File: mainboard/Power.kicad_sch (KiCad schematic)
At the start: 34 parts, among them IC801 LP5907MFX-2.8, IC802 LP5907MFX-1.5, IC803 TPS62823DLC, IC804 LP5907MFX-3.0, IC805 LP5907MFX-2.8, IC806 LP5907MFX-1.2, SW801 On / Off

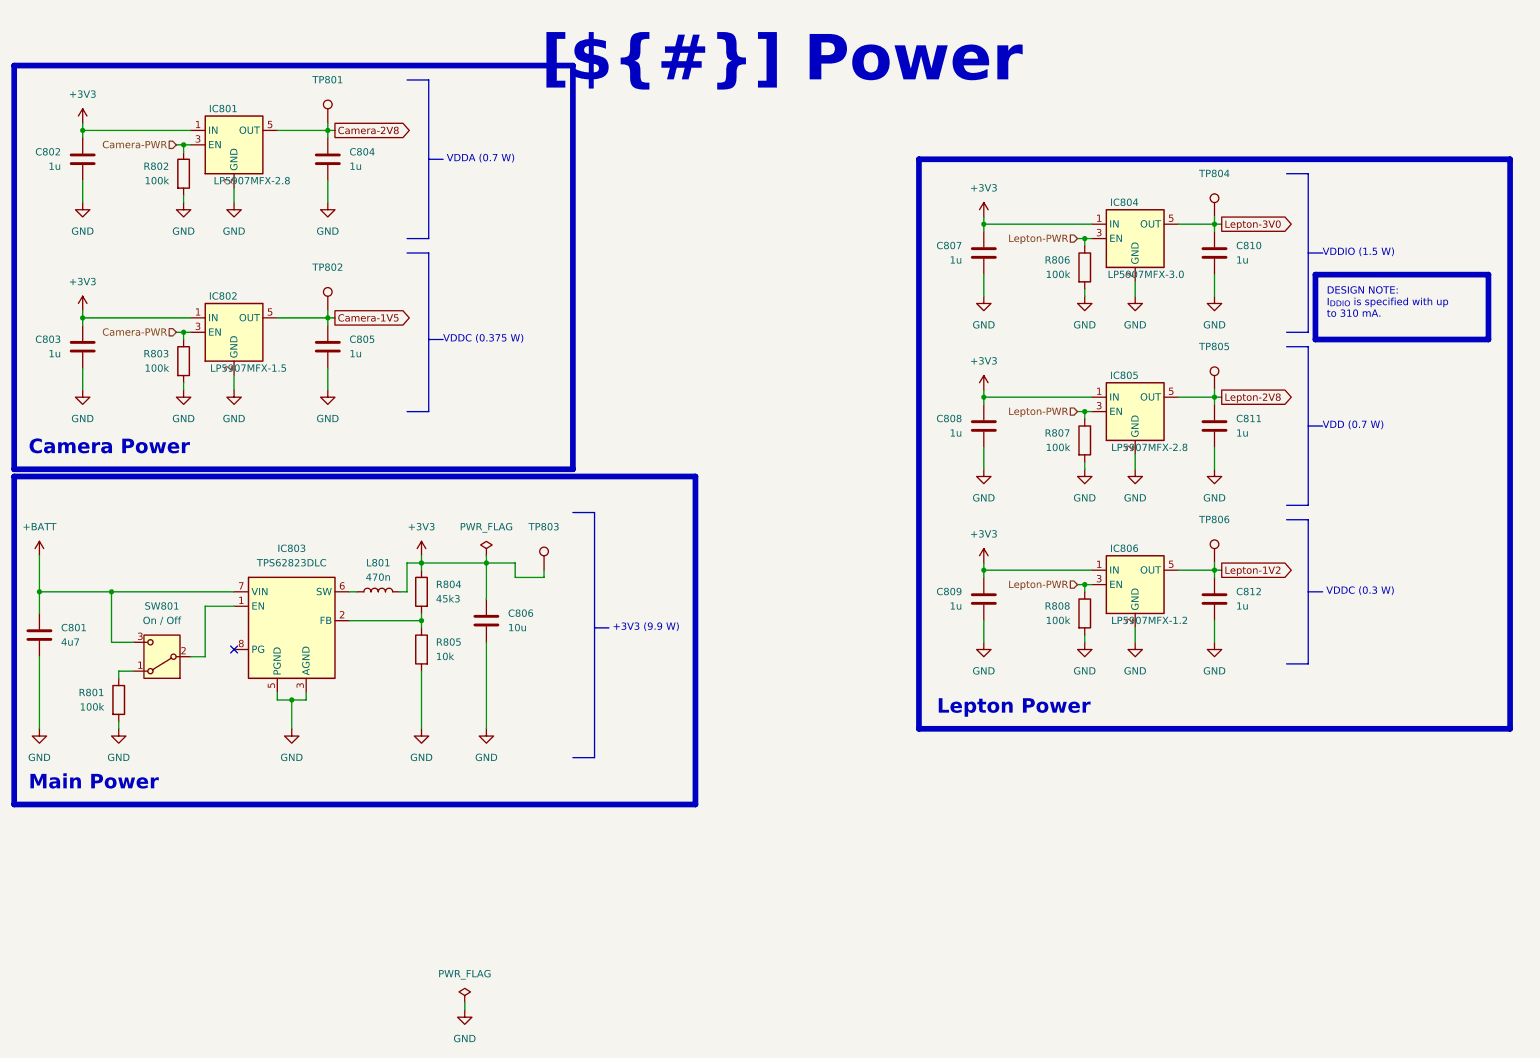
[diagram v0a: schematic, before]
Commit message: Changed: Fix different minor assembly ToDos
Signed-off-by: Daniel Kampert <DanielKampert@kampis-elektroecke.de>
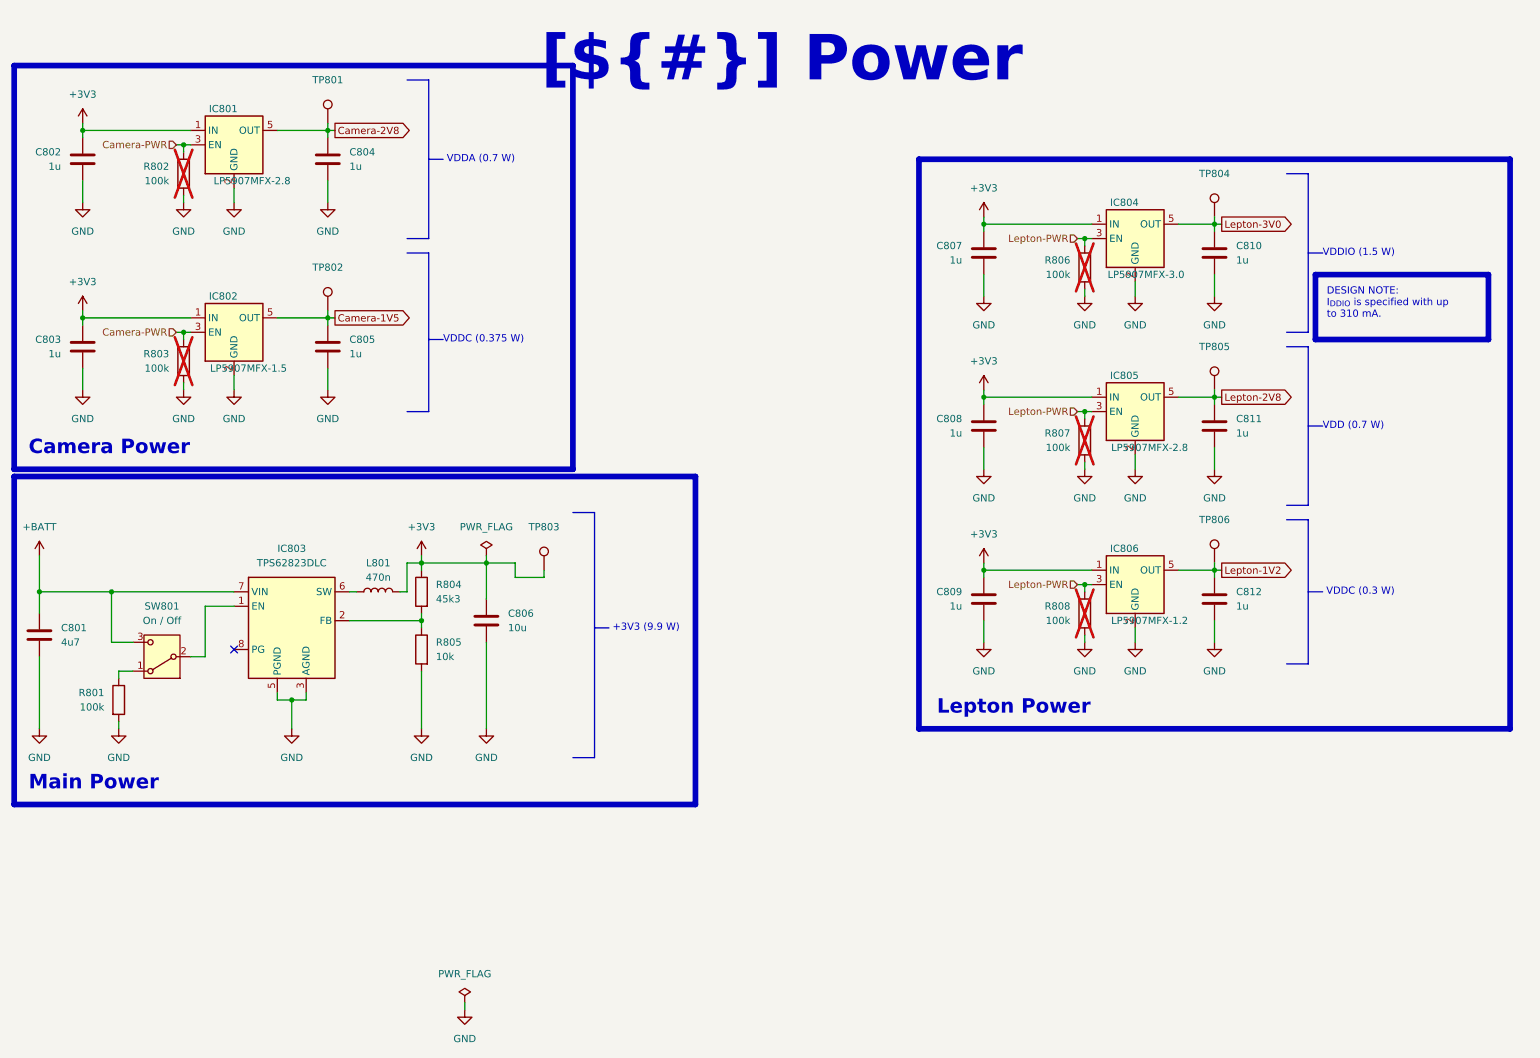
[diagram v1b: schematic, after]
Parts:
- C801: manf# 0603ZG475ZAT2A -> 06036D475MAT4A; mouser# 581-0603ZG475ZAT2A -> 581-06036D475MAT4A
- C806: manf# 0603YD106MAT2A -> 06034D106KAT2A; mouser# 581-0603YD106MAT2A -> 581-06034D106K
- R802, R803, R806, R807, R808: now not fitted; now left out of the parts list
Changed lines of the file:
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@@
 			)
 		)
-		(property "Datasheet" "https://datasheets.kyocera-avx.com/KGM_Y5V.pdf"
+		(property "Datasheet" "https://datasheets.kyocera-avx.com/cx5r.pdf"
 			(at 17.78 124.46 0)
 			(effects
@@
 			)
 		)
-		(property "manf#" "0603ZG475ZAT2A"
+		(property "manf#" "06036D475MAT4A"
 			(at 17.78 124.46 0)
 			(effects
@@
 			)
 		)
-		(property "mouser#" "581-0603ZG475ZAT2A"
+		(property "mouser#" "581-06036D475MAT4A"
 			(at 17.78 124.46 0)
 			(effects
@@
 		(unit 1)
 		(exclude_from_sim no)
-		(in_bom yes)
+		(in_bom no)
 		(on_board yes)
-		(dnp no)
+		(dnp yes)
 		(property "Reference" "R806"
 			(at 199.39 58.42 0)
@@
 		(unit 1)
 		(exclude_from_sim no)
-		(in_bom yes)
+		(in_bom no)
 		(on_board yes)
-		(dnp no)
+		(dnp yes)
 		(property "Reference" "R808"
 			(at 199.39 119.38 0)
@@
 			)
 		)
-		(property "Datasheet" "https://datasheets.kyocera-avx.com/cx5r-KGM.pdf"
+		(property "Datasheet" "https://datasheets.kyocera-avx.com/cx5r.pdf"
 			(at 96.52 121.92 0)
 			(effects
@@
 			)
 		)
-		(property "manf#" "0603YD106MAT2A"
+		(property "manf#" "06034D106KAT2A"
 			(at 96.52 121.92 0)
 			(effects
@@
 			)
 		)
-		(property "mouser#" "581-0603YD106MAT2A"
+		(property "mouser#" "581-06034D106K"
 			(at 96.52 121.92 0)
 			(effects
@@
 		(unit 1)
 		(exclude_from_sim no)
-		(in_bom yes)
+		(in_bom no)
 		(on_board yes)
-		(dnp no)
+		(dnp yes)
 		(property "Reference" "R802"
 			(at 40.64 41.91 0)
@@
 		(unit 1)
 		(exclude_from_sim no)
-		(in_bom yes)
+		(in_bom no)
 		(on_board yes)
-		(dnp no)
+		(dnp yes)
 		(property "Reference" "R803"
 			(at 40.64 74.93 0)
@@
 		(unit 1)
 		(exclude_from_sim no)
-		(in_bom yes)
+		(in_bom no)
 		(on_board yes)
-		(dnp no)
+		(dnp yes)
 		(property "Reference" "R807"
 			(at 199.39 88.9 0)

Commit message: Update to KiCad 10
Closes: #31, #29, #27

Signed-off-by: Daniel Kampert <DanielKampert@kampis-elektroecke.de>
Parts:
- TP801, TP802, TP803, TP804, TP805, TP806: value ~ -> (none)
